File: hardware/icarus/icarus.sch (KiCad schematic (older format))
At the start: 51 parts, among them J1 USB_B_Micro, J10 PWM2, J11 PWM4, J12 PWM6, J13 PWM8, J2 SWJ-DP, J3 PWR, J4 COMM, J5 GPIO, J6 PWM1, J7 PWM3, J8 PWM5, J9 PWM7, SW1 RST, SW2 BOOT, U1 STM32F407ZGTx, U2 AP2112K-3.3, U3 MPU-6050, Y1 12MHz

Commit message: Design with stm32f3
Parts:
- removed C10, C11, C12, C13, C14, C16, C18, C20, C22: 100nF, Capacitor_SMD:C_0805_2012Metric, symbol Device:C
- removed C4, C6: 2.2uF, Capacitor_SMD:C_0805_2012Metric, symbol Device:C
- removed J10: PWM2, Connector_PinHeader_2.54mm:PinHeader_1x03_P2.54mm_Vertical, symbol Connector_Generic:Conn_01x03
- removed J11: PWM4, Connector_PinHeader_2.54mm:PinHeader_1x03_P2.54mm_Vertical, symbol Connector_Generic:Conn_01x03
- removed J12: PWM6, Connector_PinHeader_2.54mm:PinHeader_1x03_P2.54mm_Vertical, symbol Connector_Generic:Conn_01x03
- removed J13: PWM8, Connector_PinHeader_2.54mm:PinHeader_1x03_P2.54mm_Vertical, symbol Connector_Generic:Conn_01x03
- removed J5: GPIO, Connector_PinHeader_2.54mm:PinHeader_1x08_P2.54mm_Vertical, symbol Connector_Generic:Conn_01x08
- removed J6: PWM1, Connector_PinHeader_2.54mm:PinHeader_1x03_P2.54mm_Vertical, symbol Connector_Generic:Conn_01x03
- removed J7: PWM3, Connector_PinHeader_2.54mm:PinHeader_1x03_P2.54mm_Vertical, symbol Connector_Generic:Conn_01x03
- removed J8: PWM5, Connector_PinHeader_2.54mm:PinHeader_1x03_P2.54mm_Vertical, symbol Connector_Generic:Conn_01x03
- removed J9: PWM7, Connector_PinHeader_2.54mm:PinHeader_1x03_P2.54mm_Vertical, symbol Connector_Generic:Conn_01x03
- removed U1: STM32F407ZGTx, Package_QFP:LQFP-144_20x20mm_P0.5mm, symbol MCU_ST_STM32F4:STM32F407ZGTx
- added J5: COMMS, Connector_PinSocket_2.54mm:PinSocket_1x06_P2.54mm_Vertical, symbol Connector_Generic:Conn_01x06
- added J6: GPIO, Connector_PinSocket_2.54mm:PinSocket_1x08_P2.54mm_Vertical, symbol Connector_Generic:Conn_01x08
- added U1: STM32F302C8Tx, Package_QFP:LQFP-48_7x7mm_P0.5mm, symbol MCU_ST_STM32F3:STM32F302C8Tx
- D3: LCSC C2296 -> C434432
- J3: footprint Connector_PinHeader_2.54mm:PinHeader_1x06_P2.54mm_Vertical -> Connector_PinSocket_2.54mm:PinSocket_1x06_P2.54mm_Vertical
- J4: value COMM -> PWM; footprint Connector_PinHeader_2.54mm:PinHeader_1x06_P2.54mm_Vertical -> Connector_PinSocket_2.54mm:PinSocket_1x06_P2.54mm_Vertical
- renumbered C19 to C10, C21 to C11, C7 to C4, C8 to C6, C9 to C7, C15 to C8, C17 to C9
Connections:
- net usart3_rx is gone; now on net pwm3: J4.3 (Pin_3)
- net usart3_tx is gone; now on net pwm4: J4.4 (Pin_4)
- net +3V3: now also U1.1 (VBAT), U1.24 (VDD), U1.36 (VDD), U1.48 (VDD), U1.9 (VDDA)
- net GND: now also U1.23 (VSS), U1.35 (VSS), U1.47 (VSS), U1.8 (VSSA)
- net boot0: now also U1.44 (BOOT0)
- net gpio1: now also J6.1 (Pin_1), U1.45 (PB8)
- net gpio2: now also J6.2 (Pin_2), U1.46 (PB9)
- net gpio3: now also J6.3 (Pin_3), U1.21 (PB10)
- net gpio4: now also J6.4 (Pin_4), U1.22 (PB11)
- net gpio5: now also J6.5 (Pin_5), U1.25 (PB12)
- net imu_int: now also U1.41 (PB5)
- net led1: now also U1.14 (PA4)
- net led2: now also U1.15 (PA5)
- net nreset: now also U1.7 (NRST)
- net osc_in: now also U1.5 (PF0)
- net osc_out: now also U1.6 (PF1)
- net pwm1: now also J4.1 (Pin_1), U1.10 (PA0)
- net pwm2: now also J4.2 (Pin_2), U1.11 (PA1)
- net pwm3: now also U1.12 (PA2)
- net pwm4: now also U1.13 (PA3)
- net pwm5: now also J4.5 (Pin_5), U1.16 (PA6)
- net pwm6: now also J4.6 (Pin_6), U1.17 (PA7)
- net scl: now also J5.6 (Pin_6), U1.42 (PB6); no longer J4.6 (Pin_6)
- net sda: now also J5.5 (Pin_5), U1.43 (PB7); no longer J4.5 (Pin_5)
- net usart2_rx: now also J5.3 (Pin_3), U1.40 (PB4); no longer J4.1 (Pin_1)
- net usart2_tx: now also J5.4 (Pin_4), U1.39 (PB3); no longer J4.2 (Pin_2)
- net usb_fs_dm: now also U1.32 (PA11)
- net usb_fs_dp: now also U1.33 (PA12)
- net jtck_swclk renamed swclk
- net swclk: now also U1.37 (PA14)
- net jtdi: no longer names the net of J2.8 (NC/TDI)
- net jtdo: no longer names the net of J2.6 (SWO/TDO)
- net jtms_swdio renamed swdio
- net swdio: now also U1.34 (PA13)
- new net miso: J6.7 (Pin_7), U1.27 (PB14)
- new net mosi: J6.8 (Pin_8), U1.28 (PB15)
- new net sck: J6.6 (Pin_6), U1.26 (PB13)
- new net usart1_rx: J5.1 (Pin_1), U1.31 (PA10)
- new net usart1_tx: J5.2 (Pin_2), U1.30 (PA9)
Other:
- note added: "Boot to system memory:\nBOOT0 - 1\nnBOOT1 - 1\n\nBoot to main flash memory:\nBOOT0 - 0\nnBOOT1 - x"
- note removed: "Boot to system memory:\nBOOT0 - 1\nBOOT1 - 0\n\nBoot to main flash memory:\nBOOT0 - 0\nBOOT1 - 0"
- moved on the sheet: C5, C6, C7

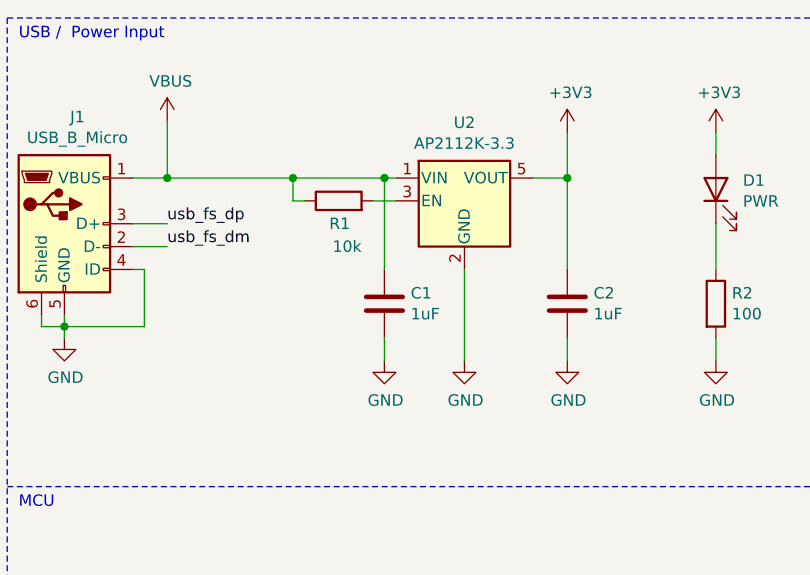
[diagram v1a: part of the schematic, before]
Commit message: Switch linear regulator
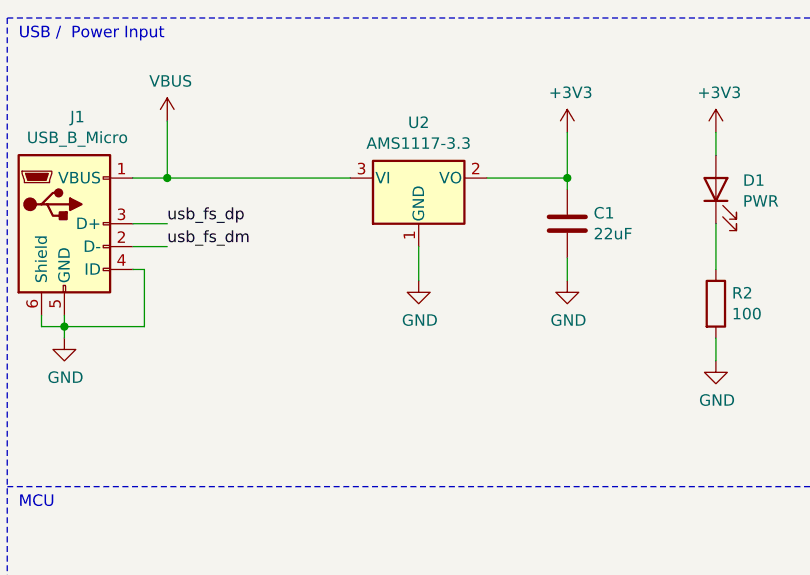
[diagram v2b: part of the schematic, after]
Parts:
- removed C2: 1uF, Capacitor_SMD:C_0805_2012Metric, symbol Device:C
- removed R1: 10k, Resistor_SMD:R_0805_2012Metric, symbol Device:R
- removed U2: AP2112K-3.3, Package_TO_SOT_SMD:SOT-23-5, symbol Regulator_Linear:AP2112K-3.3
- added U2: AMS1117-3.3, Package_TO_SOT_SMD:SOT-223-3_TabPin2, symbol Regulator_Linear:AMS1117-3.3
- C1: value 1uF -> 22uF; footprint Capacitor_SMD:C_0805_2012Metric -> Capacitor_Tantalum_SMD:CP_EIA-3216-18_Kemet-A; LCSC C28323 -> C116575
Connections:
- net +3V3: now also C1.1, U2.2 (VO)
- net GND: now also U2.1 (GND)
- net VBUS: now also U2.3 (VI); no longer C1.1
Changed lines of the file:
@@
 	1050 1200 1200 1200
-$Comp
-L Regulator_Linear:AP2112K-3.3 U2
-U 1 1 6167ED31
-P 2500 1300
-F 0 "U2" H 2500 1642 50  0000 C CNN
-F 1 "AP2112K-3.3" H 2500 1551 50  0000 C CNN
-F 2 "Package_TO_SOT_SMD:SOT-23-5" H 2500 1625 50  0001 C CNN
-F 3 "https://www.diodes.com/assets/Datasheets/AP2112.pdf" H 2500 1400 50  0001 C CNN
-F 4 "C51118" H 2500 1300 50  0001 C CNN "LCSC"
-	1    2500 1300
-	1    0    0    -1
-$EndComp
 $Comp
 L power:+3V3 #PWR07
@@
 	1    0    0    -1
 $EndComp
-Wire Wire Line
-	2800 1200 2950 1200
-Wire Wire Line
-	2950 1200 2950 1000
-$Comp
-L power:GND #PWR06
-U 1 1 61687457
-P 2500 2000
-F 0 "#PWR06" H 2500 1750 50  0001 C CNN
-F 1 "GND" H 2505 1827 50  0000 C CNN
-F 2 "" H 2500 2000 50  0001 C CNN
-F 3 "" H 2500 2000 50  0001 C CNN
-	1    2500 2000
-	1    0    0    -1
-$EndComp
-$Comp
-L Device:R R1
-U 1 1 6168FB48
-P 1950 1300
-F 0 "R1" V 1850 1250 50  0000 L CNN
-F 1 "10k" V 1750 1200 50  0000 L CNN
-F 2 "Resistor_SMD:R_0805_2012Metric" V 1880 1300 50  0001 C CNN
-F 3 "~" H 1950 1300 50  0001 C CNN
-F 4 "C17414" V 1950 1300 50  0001 C CNN "LCSC"
-	1    1950 1300
-	0    -1   -1   0
-$EndComp
-Wire Wire Line
-	2200 1300 2100 1300
-Wire Wire Line
-	2200 1200 2150 1200
-Wire Wire Line
-	1800 1300 1750 1300
-Wire Wire Line
-	1750 1300 1750 1200
-Connection ~ 1750 1200
 Connection ~ 1200 1200
-Wire Wire Line
-	1200 1200 1750 1200
-$Comp
-L Device:C C2
-U 1 1 616AAC74
-P 2950 1750
-F 0 "C2" H 3065 1796 50  0000 L CNN
-F 1 "1uF" H 3065 1705 50  0000 L CNN
-F 2 "Capacitor_SMD:C_0805_2012Metric" H 2988 1600 50  0001 C CNN
-F 3 "~" H 2950 1750 50  0001 C CNN
-F 4 "C28323" H 2950 1750 50  0001 C CNN "LCSC"
-	1    2950 1750
-	1    0    0    -1
-$EndComp
-$Comp
-L Device:C C1
-U 1 1 616AC4D6
-P 2150 1750
-F 0 "C1" H 2265 1796 50  0000 L CNN
-F 1 "1uF" H 2265 1705 50  0000 L CNN
-F 2 "Capacitor_SMD:C_0805_2012Metric" H 2188 1600 50  0001 C CNN
-F 3 "~" H 2150 1750 50  0001 C CNN
-F 4 "C28323" H 2150 1750 50  0001 C CNN "LCSC"
-	1    2150 1750
-	1    0    0    -1
-$EndComp
-$Comp
-L power:GND #PWR03
-U 1 1 616AF64E
-P 2150 2000
-F 0 "#PWR03" H 2150 1750 50  0001 C CNN
-F 1 "GND" H 2155 1827 50  0000 C CNN
-F 2 "" H 2150 2000 50  0001 C CNN
-F 3 "" H 2150 2000 50  0001 C CNN
-	1    2150 2000
-	1    0    0    -1
-$EndComp
-$Comp
-L power:GND #PWR08
-U 1 1 616AFCC4
-P 2950 2000
-F 0 "#PWR08" H 2950 1750 50  0001 C CNN
-F 1 "GND" H 2955 1827 50  0000 C CNN
-F 2 "" H 2950 2000 50  0001 C CNN
-F 3 "" H 2950 2000 50  0001 C CNN
-	1    2950 2000
-	1    0    0    -1
-$EndComp
-Wire Wire Line
-	2500 1600 2500 2000
-Wire Wire Line
-	2950 2000 2950 1900
-Wire Wire Line
-	2150 2000 2150 1900
-Wire Wire Line
-	2150 1600 2150 1200
-Connection ~ 2150 1200
-Wire Wire Line
-	2150 1200 1750 1200
-Wire Wire Line
-	2950 1600 2950 1200
-Connection ~ 2950 1200
 $Comp
 L Device:LED D1
@@
 Text Label 1400 6550 2    50   ~ 0
 imu_int
+$Comp
+L Regulator_Linear:AMS1117-3.3 U2
+U 1 1 6186545C
+P 2300 1200
+F 0 "U2" H 2300 1442 50  0000 C CNN
+F 1 "AMS1117-3.3" H 2300 1351 50  0000 C CNN
+F 2 "Package_TO_SOT_SMD:SOT-223-3_TabPin2" H 2300 1400 50  0001 C CNN
+F 3 "http://www.advanced-monolithic.com/pdf/ds1117.pdf" H 2400 950 50  0001 C CNN
+F 4 "C6186" H 2300 1200 50  0001 C CNN "LCSC"
+	1    2300 1200
+	1    0    0    -1
+$EndComp
+$Comp
+L Device:C C1
+U 1 1 618666FA
+P 2950 1400
+F 0 "C1" H 3065 1446 50  0000 L CNN
+F 1 "22uF" H 3065 1355 50  0000 L CNN
+F 2 "Capacitor_Tantalum_SMD:CP_EIA-3216-18_Kemet-A" H 2988 1250 50  0001 C CNN
+F 3 "~" H 2950 1400 50  0001 C CNN
+F 4 "C116575" H 2950 1400 50  0001 C CNN "LCSC"
+	1    2950 1400
+	1    0    0    -1
+$EndComp
+Wire Wire Line
+	1200 1200 2000 1200
+$Comp
+L power:GND #PWR0101
+U 1 1 61881528
+P 2300 1650
+F 0 "#PWR0101" H 2300 1400 50  0001 C CNN
+F 1 "GND" H 2305 1477 50  0000 C CNN
+F 2 "" H 2300 1650 50  0001 C CNN
+F 3 "" H 2300 1650 50  0001 C CNN
+	1    2300 1650
+	1    0    0    -1
+$EndComp
+$Comp
+L power:GND #PWR0102
+U 1 1 618818D9
+P 2950 1650
+F 0 "#PWR0102" H 2950 1400 50  0001 C CNN
+F 1 "GND" H 2955 1477 50  0000 C CNN
+F 2 "" H 2950 1650 50  0001 C CNN
+F 3 "" H 2950 1650 50  0001 C CNN
+	1    2950 1650
+	1    0    0    -1
+$EndComp
+Wire Wire Line
+	2300 1500 2300 1650
+Wire Wire Line
+	2600 1200 2950 1200
+Wire Wire Line
+	2950 1200 2950 1250
+Wire Wire Line
+	2950 1000 2950 1200
+Connection ~ 2950 1200
+Wire Wire Line
+	2950 1550 2950 1650
 $EndSCHEMATC

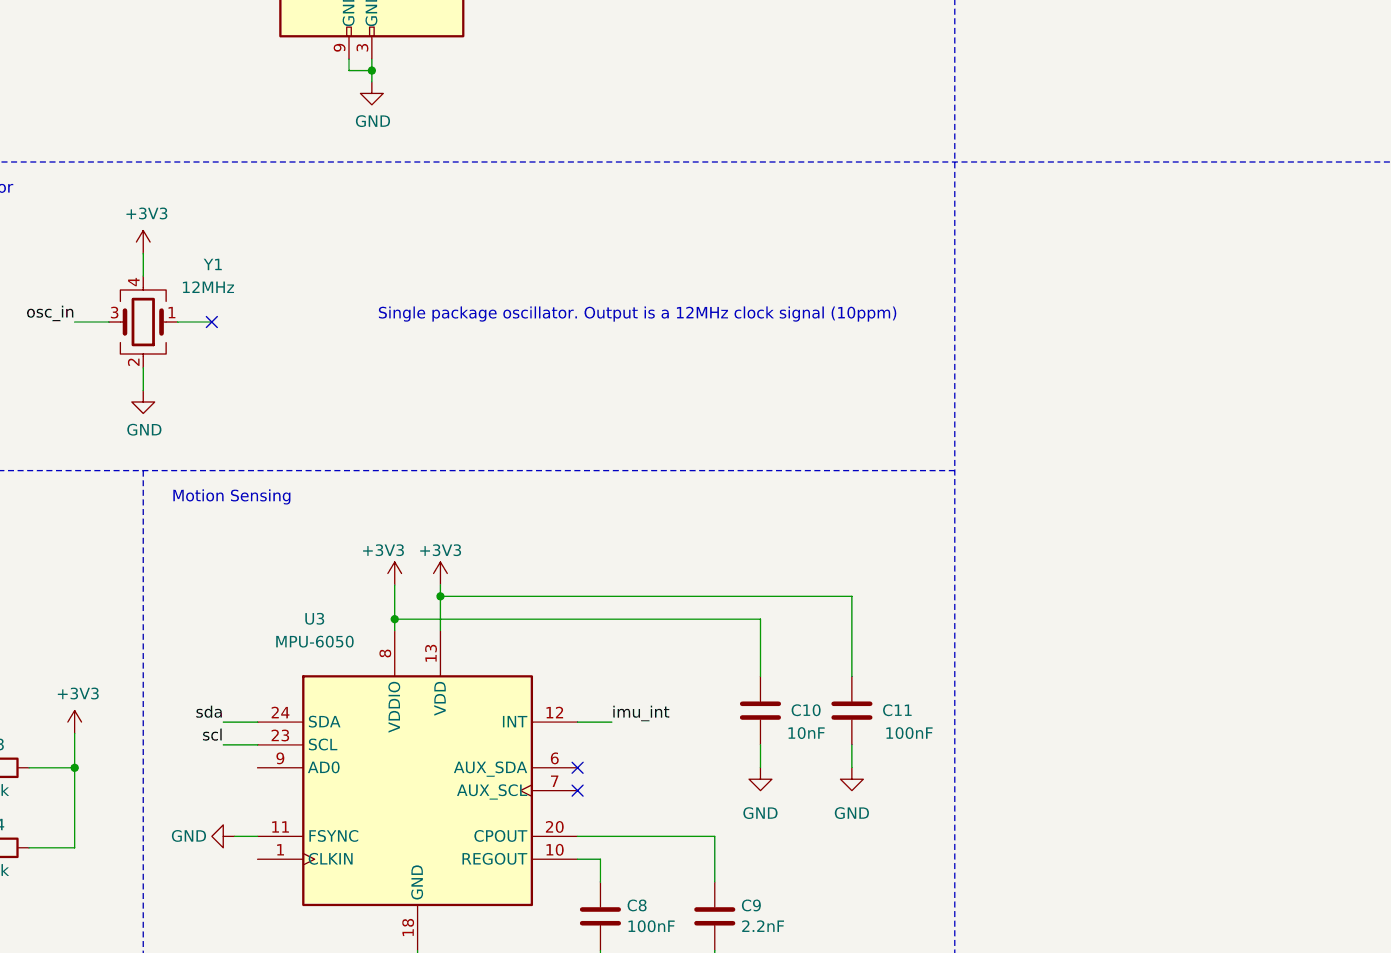
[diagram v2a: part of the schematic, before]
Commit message: Resolves #2, #9, #10. Test points, USART1 Labels, IMU AD0 pint.
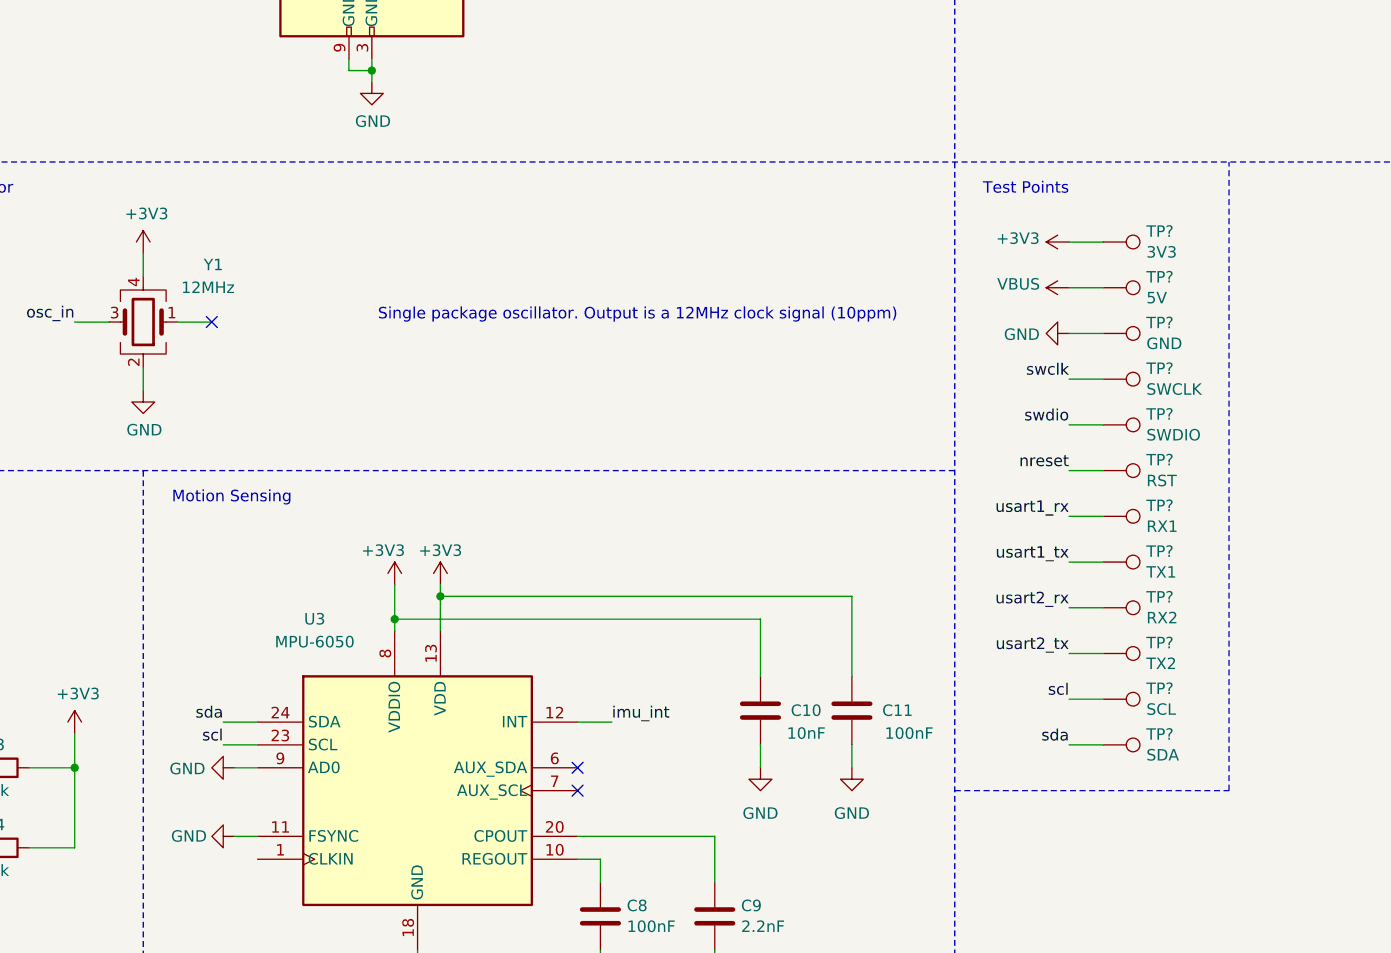
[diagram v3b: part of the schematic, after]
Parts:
- added TP?: 3V3, symbol Connector:TestPoint
- added TP?: 5V, symbol Connector:TestPoint
- added TP?: GND, symbol Connector:TestPoint
- added TP?: SWCLK, symbol Connector:TestPoint
- added TP?: SWDIO, symbol Connector:TestPoint
- added TP?: RX1, symbol Connector:TestPoint
- added TP?: TX1, symbol Connector:TestPoint
- added TP?: RX2, symbol Connector:TestPoint
- added TP?: TX2, symbol Connector:TestPoint
- added TP?: SCL, symbol Connector:TestPoint
- added TP?: SDA, symbol Connector:TestPoint
- added TP?: RST, symbol Connector:TestPoint
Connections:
- net +3V3: now also TP?.1
- net GND: now also U3.9 (AD0), TP?.1
- net VBUS: now also TP?.1
- net nreset: now also TP?.1
- net scl: now also TP?.1
- net sda: now also TP?.1
- net swclk: now also TP?.1
- net swdio: now also TP?.1
- net usart1_rx: now also TP?.1
- net usart1_tx: now also TP?.1
- net usart2_rx: now also TP?.1
- net usart2_tx: now also TP?.1
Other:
- note added: "Test Points"
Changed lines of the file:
@@
 Wire Wire Line
 	2950 1550 2950 1650
+$Comp
+L Connector:TestPoint TP?
+U 1 1 61B20520
+P 9550 6350
+F 0 "TP?" V 9504 6538 50  0000 L CNN
+F 1 "3V3" V 9595 6538 50  0000 L CNN
+F 2 "" H 9750 6350 50  0001 C CNN
+F 3 "~" H 9750 6350 50  0001 C CNN
+	1    9550 6350
+	0    1    1    0
+$EndComp
+$Comp
+L Connector:TestPoint TP?
+U 1 1 61B28D83
+P 9550 6550
+F 0 "TP?" V 9504 6738 50  0000 L CNN
+F 1 "5V" V 9595 6738 50  0000 L CNN
+F 2 "" H 9750 6550 50  0001 C CNN
+F 3 "~" H 9750 6550 50  0001 C CNN
+	1    9550 6550
+	0    1    1    0
+$EndComp
+$Comp
+L Connector:TestPoint TP?
+U 1 1 61B2FD8F
+P 9550 6750
+F 0 "TP?" V 9504 6938 50  0000 L CNN
+F 1 "GND" V 9595 6938 50  0000 L CNN
+F 2 "" H 9750 6750 50  0001 C CNN
+F 3 "~" H 9750 6750 50  0001 C CNN
+	1    9550 6750
+	0    1    1    0
+$EndComp
+$Comp
+L Connector:TestPoint TP?
+U 1 1 61B37A6F
+P 9550 6950
+F 0 "TP?" V 9504 7138 50  0000 L CNN
+F 1 "SWCLK" V 9595 7138 50  0000 L CNN
+F 2 "" H 9750 6950 50  0001 C CNN
+F 3 "~" H 9750 6950 50  0001 C CNN
+	1    9550 6950
+	0    1    1    0
+$EndComp
+$Comp
+L Connector:TestPoint TP?
+U 1 1 61B3EC36
+P 9550 7150
+F 0 "TP?" V 9504 7338 50  0000 L CNN
+F 1 "SWDIO" V 9595 7338 50  0000 L CNN
+F 2 "" H 9750 7150 50  0001 C CNN
+F 3 "~" H 9750 7150 50  0001 C CNN
+	1    9550 7150
+	0    1    1    0
+$EndComp
+Wire Wire Line
+	9550 6350 9400 6350
+Wire Wire Line
+	9550 6550 9400 6550
+Wire Wire Line
+	9550 6750 9400 6750
+Wire Wire Line
+	9550 6950 9400 6950
+Wire Wire Line
+	9550 7150 9400 7150
+$Comp
+L power:+3V3 #PWR?
+U 1 1 61B6D164
+P 9400 6350
+F 0 "#PWR?" H 9400 6200 50  0001 C CNN
+F 1 "+3V3" V 9415 6478 50  0000 L CNN
+F 2 "" H 9400 6350 50  0001 C CNN
+F 3 "" H 9400 6350 50  0001 C CNN
+	1    9400 6350
+	0    -1   -1   0
+$EndComp
+$Comp
+L power:VBUS #PWR?
+U 1 1 61B6ED39
+P 9400 6550
+F 0 "#PWR?" H 9400 6400 50  0001 C CNN
+F 1 "VBUS" V 9415 6677 50  0000 L CNN
+F 2 "" H 9400 6550 50  0001 C CNN
+F 3 "" H 9400 6550 50  0001 C CNN
+	1    9400 6550
+	0    -1   -1   0
+$EndComp
+$Comp
+L power:GND #PWR?
+U 1 1 61B6FBBA
+P 9400 6750
+F 0 "#PWR?" H 9400 6500 50  0001 C CNN
+F 1 "GND" V 9405 6622 50  0000 R CNN
+F 2 "" H 9400 6750 50  0001 C CNN
+F 3 "" H 9400 6750 50  0001 C CNN
+	1    9400 6750
+	0    1    1    0
+$EndComp
+Text Label 9400 6950 2    50   ~ 0
+swclk
+Text Label 9400 7150 2    50   ~ 0
+swdio
+$Comp
+L Connector:TestPoint TP?
+U 1 1 61B7295E
+P 9550 7550
+F 0 "TP?" V 9504 7738 50  0000 L CNN
+F 1 "RX1" V 9595 7738 50  0000 L CNN
+F 2 "" H 9750 7550 50  0001 C CNN
+F 3 "~" H 9750 7550 50  0001 C CNN
+	1    9550 7550
+	0    1    1    0
+$EndComp
+$Comp
+L Connector:TestPoint TP?
+U 1 1 61B8B0FD
+P 9550 7750
+F 0 "TP?" V 9504 7938 50  0000 L CNN
+F 1 "TX1" V 9595 7938 50  0000 L CNN
+F 2 "" H 9750 7750 50  0001 C CNN
+F 3 "~" H 9750 7750 50  0001 C CNN
+	1    9550 7750
+	0    1    1    0
+$EndComp
+Wire Wire Line
+	9550 7550 9400 7550
+Wire Wire Line
+	9550 7750 9400 7750
+Text Label 9400 7550 2    50   ~ 0
+usart1_rx
+Text Label 9400 7750 2    50   ~ 0
+usart1_tx
+$Comp
+L Connector:TestPoint TP?
+U 1 1 61BA44C6
+P 9550 7950
+F 0 "TP?" V 9504 8138 50  0000 L CNN
+F 1 "RX2" V 9595 8138 50  0000 L CNN
+F 2 "" H 9750 7950 50  0001 C CNN
+F 3 "~" H 9750 7950 50  0001 C CNN
+	1    9550 7950
+	0    1    1    0
+$EndComp
+$Comp
+L Connector:TestPoint TP?
+U 1 1 61BA44CC
+P 9550 8150
+F 0 "TP?" V 9504 8338 50  0000 L CNN
+F 1 "TX2" V 9595 8338 50  0000 L CNN
+F 2 "" H 9750 8150 50  0001 C CNN
+F 3 "~" H 9750 8150 50  0001 C CNN
+	1    9550 8150
+	0    1    1    0
+$EndComp
+Wire Wire Line
+	9550 7950 9400 7950
+Wire Wire Line
+	9550 8150 9400 8150
+Text Label 9400 7950 2    50   ~ 0
+usart2_rx
+Text Label 9400 8150 2    50   ~ 0
+usart2_tx
+$Comp
+L Connector:TestPoint TP?
+U 1 1 61BAE113
+P 9550 8350
+F 0 "TP?" V 9504 8538 50  0000 L CNN
+F 1 "SCL" V 9595 8538 50  0000 L CNN
+F 2 "" H 9750 8350 50  0001 C CNN
+F 3 "~" H 9750 8350 50  0001 C CNN
+	1    9550 8350
+	0    1    1    0
+$EndComp
+$Comp
+L Connector:TestPoint TP?
+U 1 1 61BAE119
+P 9550 8550
+F 0 "TP?" V 9504 8738 50  0000 L CNN
+F 1 "SDA" V 9595 8738 50  0000 L CNN
+F 2 "" H 9750 8550 50  0001 C CNN
+F 3 "~" H 9750 8550 50  0001 C CNN
+	1    9550 8550
+	0    1    1    0
+$EndComp
+Wire Wire Line
+	9550 8350 9400 8350
+Wire Wire Line
+	9550 8550 9400 8550
+Text Label 9400 8350 2    50   ~ 0
+scl
+Text Label 9400 8550 2    50   ~ 0
+sda
+$Comp
+L power:GND #PWR?
+U 1 1 61BB6C33
+P 5750 8650
+F 0 "#PWR?" H 5750 8400 50  0001 C CNN
+F 1 "GND" V 5755 8522 50  0000 R CNN
+F 2 "" H 5750 8650 50  0001 C CNN
+F 3 "" H 5750 8650 50  0001 C CNN
+	1    5750 8650
+	0    1    1    0
+$EndComp
+Wire Wire Line
+	5850 8650 5750 8650
+Text Notes 9400 6150 2    50   ~ 0
+Test Points
+$Comp
+L Connector:TestPoint TP?
+U 1 1 61BF1D61
+P 9550 7350
+F 0 "TP?" V 9504 7538 50  0000 L CNN
+F 1 "RST" V 9595 7538 50  0000 L CNN
+F 2 "" H 9750 7350 50  0001 C CNN
+F 3 "~" H 9750 7350 50  0001 C CNN
+	1    9550 7350
+	0    1    1    0
+$EndComp
+Wire Wire Line
+	9550 7350 9400 7350
+Text Label 9400 7350 2    50   ~ 0
+nreset
+Wire Notes Line
+	8900 8750 10100 8750
+Wire Notes Line
+	10100 8750 10100 6000
 $EndSCHEMATC
